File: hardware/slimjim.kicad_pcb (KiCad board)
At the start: 2 copper layers, 7 parts, among them J1 USB, P1 CONN_01X12, P2 CONN_01X12, SW1 SW_PUSH, U1 RF200, U2 TC200

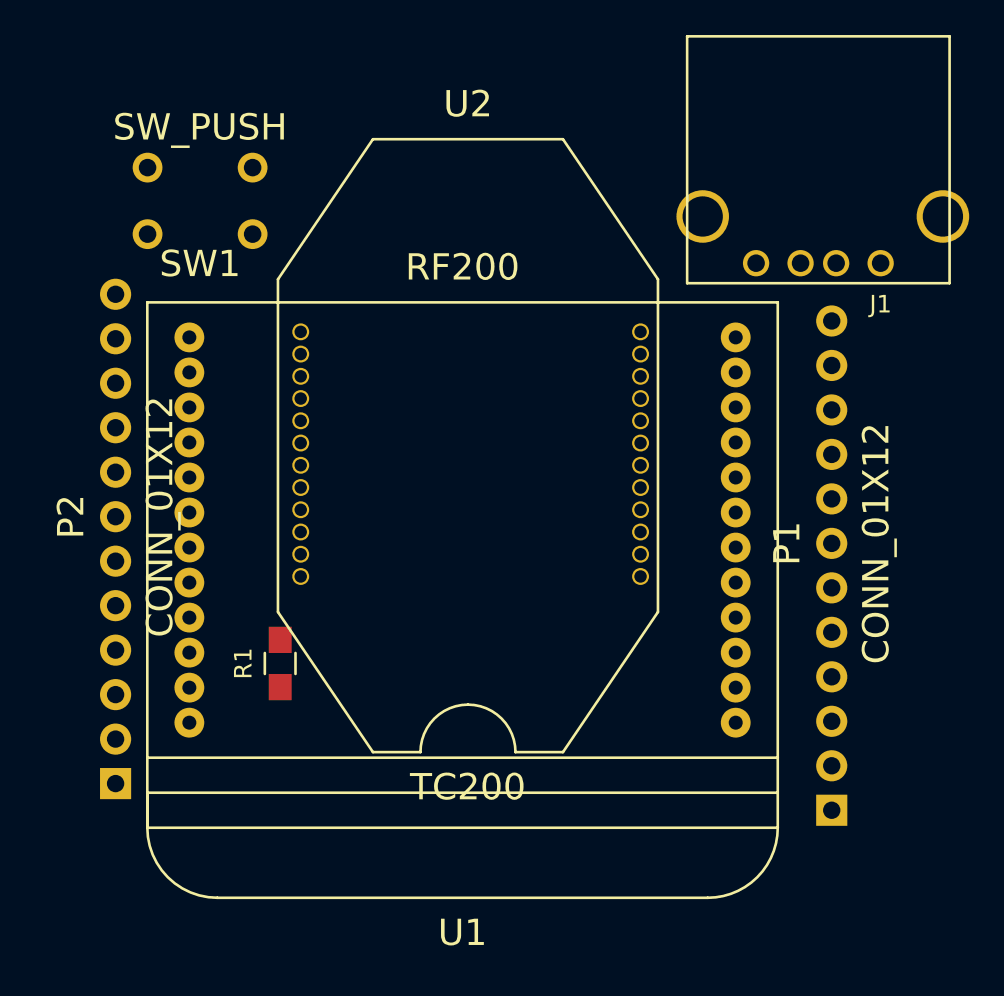
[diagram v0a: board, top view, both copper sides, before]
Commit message: Improve part placement.
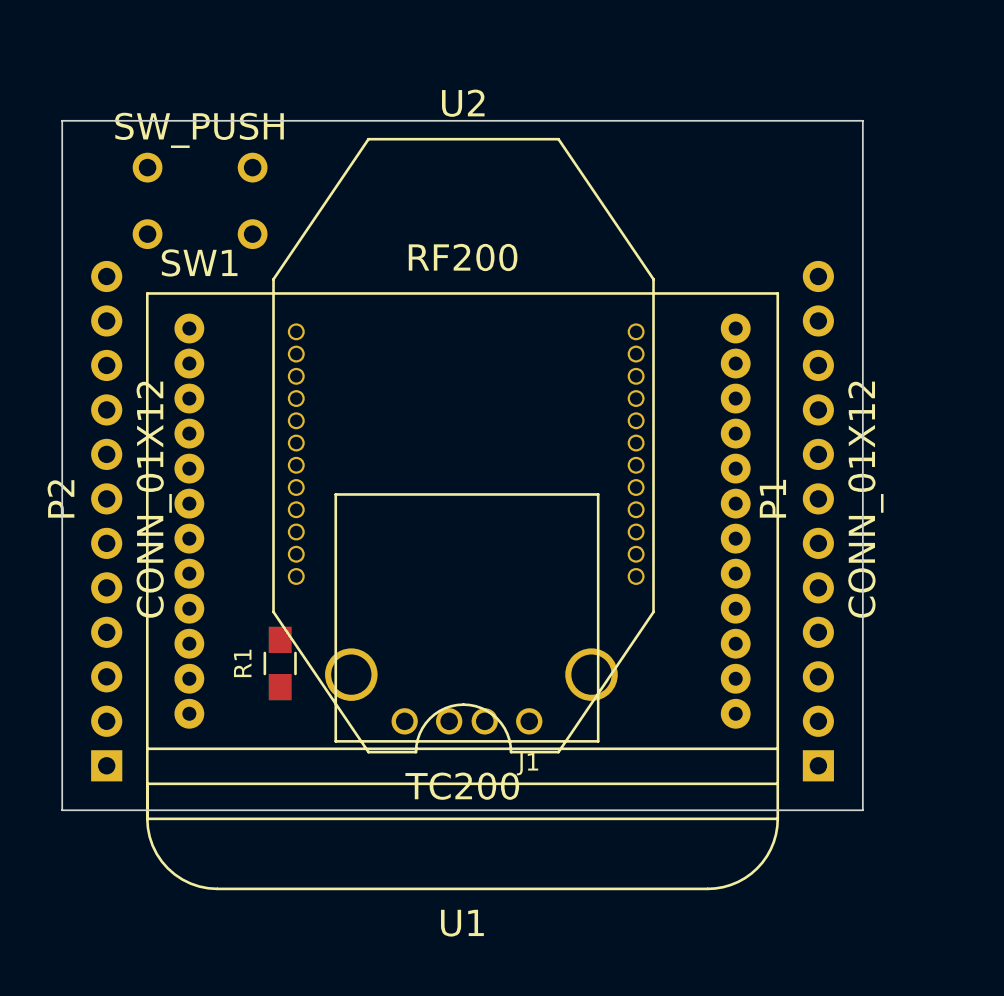
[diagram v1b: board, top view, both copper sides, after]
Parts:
- moved J1 33.0 mm to (196.8, 113.0)
- moved P1 2.65 mm to (213.4, 115.6)
- moved P2 1.14 mm to (172.7, 115.6)
- moved U1 0.51 mm to (193.0, 101.6)
- moved U2 0.25 mm to (193.0, 97.8)
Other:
- board outline added: 45.7 x 39.4 mm
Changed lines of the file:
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@@
     (links 61)
     (no_connects 61)
-    (area 0 0 0 0)
+    (area 170.129999 78.689999 215.950001 118.160001)
     (thickness 1.6)
-    (drawings 0)
+    (drawings 4)
     (tracks 0)
     (zones 0)
@@
   )
   (module Connect:USB_A (layer F.Cu)
-    (at 216.916 86.868 180)
+    (at 196.85 113.03 180)
     (descr "USB A connector")
     (tags "USB USB_A")
@@
   )
   (module _CrumpPrints:Header_1x12_100 (layer F.Cu)
-    (at 214.122 118.11 90)
+    (at 213.36 115.57 90)
     (fp_text reference P1 (at 15.24 -2.54 90) (layer F.SilkS)
       (effects (font (size 1.5 1.5) (thickness 0.15)))
@@
   )
   (module _CrumpPrints:Header_1x12_100 (layer F.Cu)
-    (at 173.228 116.586 90)
+    (at 172.72 115.57 90)
     (fp_text reference P2 (at 15.24 -2.54 90) (layer F.SilkS)
       (effects (font (size 1.5 1.5) (thickness 0.15)))
@@
   )
   (module _CrumpPrints:RF200 (layer F.Cu)
-    (at 193.04 102.108 180)
+    (at 193.04 101.6 180)
     (fp_text reference U1 (at -0.000001 -23 180) (layer F.SilkS)
       (effects (font (size 1.5 1.5) (thickness 0.15)))
@@
   )
   (module _CrumpPrints:TC200 (layer F.Cu)
-    (at 193.294 97.79)
+    (at 193.04 97.79)
     (fp_text reference U2 (at 0.05625 -20) (layer F.SilkS)
       (effects (font (size 1.5 1.5) (thickness 0.15)))
@@
       (net 13 RF_12))
   )
+  (gr_line (start 215.9 78.74) (end 215.9 118.11) (angle 90) (layer Edge.Cuts) (width 0.1))
+  (gr_line (start 170.18 78.74) (end 215.9 78.74) (angle 90) (layer Edge.Cuts) (width 0.1))
+  (gr_line (start 170.18 118.11) (end 170.18 78.74) (angle 90) (layer Edge.Cuts) (width 0.1))
+  (gr_line (start 215.9 118.11) (end 170.18 118.11) (angle 90) (layer Edge.Cuts) (width 0.1))
 )

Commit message: Initial routing.
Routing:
- net RF_24: track 0.00 -> 114.6 mm, vias 0 -> 1
- net RF_23: track 0.00 -> 75.7 mm, vias 0 -> 1
- net TC_17: track 0.00 -> 49.2 mm
- net RF_8: track 0.00 -> 42.2 mm
- net RF_5: track 0.00 -> 36.5 mm, vias 0 -> 1
- net TC_6: track 0.00 -> 35.6 mm, vias 0 -> 1
- net TC_21: track 0.00 -> 34.0 mm
- net RF_9: track 0.00 -> 32.0 mm
- net RF_22: track 0.00 -> 20.3 mm, vias 0 -> 1
- net RF_2: track 0.00 -> 13.9 mm
- net RF_3: track 0.00 -> 13.3 mm
- net RF_4: track 0.00 -> 12.8 mm
- net TC_5: track 0.00 -> 12.3 mm
- net RF_16: track 0.00 -> 12.2 mm
- net TC_1: track 0.00 -> 12.1 mm
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
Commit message: PCB cleanup.
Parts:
- added G***: LOGO, _CrumpSymbols:Symbol_OSHW-Logo_12.5mm_NoText_Silkscreen, B.Cu at (193.0, 88.9)
- SW1: value SW_PUSH -> RESET
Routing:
- added copper zone on B.Cu, net RF_24
- added copper zone on F.Cu, net RF_24
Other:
- outline, holes or cut-outs redrawn
- board text added: "@tylercrumpton"
- board text added: "CC-BY-SA 4.0"
- board text added: "SLIMJIM"
- board text added: "https://git.io/vVlPX"
- board text added: "v1.0"
